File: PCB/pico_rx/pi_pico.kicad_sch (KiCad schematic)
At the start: 18 parts, among them J3 Battery, J3 Speaker, J4 Headphone, J4 I2C Display, SW1 RotaryEncoder_Switch, SW1 SW_Push, SW2 SW_Push, SW4 SW_SPDT, U5 Pico

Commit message: Get CW working
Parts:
- added R3 (x2): 1k, Resistor_SMD:R_0805_2012Metric, symbol Device:R
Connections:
- net RX_I: now also R3.2; no longer U5.32 (GPIO27_ADC1)
- net RX_Q: now also R3.2; no longer U5.31 (GPIO26_ADC0)
- net PUSH: now reaches U5.7 (GPIO5)
- net PUSH: now also SW1.S1
- net EEPROM_SCL: no longer names the net of U5.20 (GPIO15)
- net EEPROM_SDA: no longer names the net of U5.19 (GPIO14)
- new net: R3.1, U5.31 (GPIO26_ADC0)
- new net: R3.1, U5.32 (GPIO27_ADC1)
- no-connect marks 0 -> 21
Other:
- note added: "Note: D1 must be removed from PI Pico"
- note added: "R9, C34 determine LPF cutoff 1/(2 * pi * 100 * 100e-9) ~= 16kHz"
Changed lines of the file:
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@@
   (junction (at 217.17 96.52) (diameter 0) (color 0 0 0 0)
   )
+  (no_connect (at 52.07 66.04))
+  (no_connect (at 142.24 106.68))
+  (no_connect (at 160.02 53.34))
+  (no_connect (at 160.02 68.58))
+  (no_connect (at 160.02 60.96))
+  (no_connect (at 160.02 78.74))
+  (no_connect (at 124.46 81.28))
+  (no_connect (at 124.46 99.06))
+  (no_connect (at 124.46 88.9))
+  (no_connect (at 124.46 93.98))
+  (no_connect (at 124.46 78.74))
+  (no_connect (at 88.9 166.37))
+  (no_connect (at 124.46 91.44))
+  (no_connect (at 139.7 106.68))
+  (no_connect (at 124.46 101.6))
+  (no_connect (at 160.02 71.12))
+  (no_connect (at 144.78 106.68))
+  (no_connect (at 124.46 73.66))
+  (no_connect (at 124.46 86.36))
+  (no_connect (at 124.46 76.2))
+  (no_connect (at 160.02 66.04))
   (wire (pts (xy 176.53 55.88) (xy 171.45 55.88))
     (stroke (width 0) (type default))
@@
     (stroke (width 0) (type default))
   )
-  (wire (pts (xy 107.95 101.6) (xy 124.46 101.6))
-    (stroke (width 0) (type default))
-  )
   (wire (pts (xy 160.02 58.42) (xy 165.1 58.42))
     (stroke (width 0) (type default))
@@
     (stroke (width 0) (type default))
   )
+  (wire (pts (xy 234.95 86.36) (xy 238.76 86.36))
+    (stroke (width 0) (type default))
+  )
   (wire (pts (xy 36.83 66.04) (xy 40.64 66.04))
     (stroke (width 0) (type default))
@@
     (stroke (width 0) (type default))
   )
+  (wire (pts (xy 179.07 76.2) (xy 182.88 76.2))
+    (stroke (width 0) (type default))
+  )
   (wire (pts (xy 238.76 96.52) (xy 217.17 96.52))
     (stroke (width 0) (type default))
@@
     (stroke (width 0) (type default))
   )
-  (wire (pts (xy 189.23 91.44) (xy 189.23 88.9))
-    (stroke (width 0) (type default))
-  )
   (wire (pts (xy 81.28 179.07) (xy 82.55 179.07))
     (stroke (width 0) (type default))
@@
     (stroke (width 0) (type default))
   )
+  (wire (pts (xy 179.07 73.66) (xy 182.88 73.66))
+    (stroke (width 0) (type default))
+  )
   (wire (pts (xy 105.41 63.5) (xy 124.46 63.5))
     (stroke (width 0) (type default))
@@
     (stroke (width 0) (type default))
   )
+  (wire (pts (xy 95.25 68.58) (xy 124.46 68.58))
+    (stroke (width 0) (type default))
+  )
   (wire (pts (xy 165.1 83.82) (xy 165.1 96.52))
     (stroke (width 0) (type default))
@@
   )
   (wire (pts (xy 217.17 140.97) (xy 223.52 140.97))
-    (stroke (width 0) (type default))
-  )
-  (wire (pts (xy 107.95 99.06) (xy 124.46 99.06))
     (stroke (width 0) (type default))
   )
@@
     (effects (font (size 1.27 1.27)) (justify right bottom))
   )
+  (text "Note: D1 must be removed from PI Pico" (at 121.92 43.18 0)
+    (effects (font (size 1.27 1.27)) (justify left bottom))
+  )
   (text "User Interface" (at 198.12 40.64 0)
     (effects (font (size 1.27 1.27)) (justify left bottom))
   )
-  (label "EEPROM_SCL" (at 107.95 101.6 180) (fields_autoplaced)
-    (effects (font (size 1.27 1.27)) (justify right bottom))
+  (text "R9, C34  determine LPF cutoff\n1/(2 * pi * 100 * 100e-9) ~= 16kHz"
+    (at 21.59 148.59 0)
+    (effects (font (size 2.5 2.5)) (justify left bottom))
+  )
+  (label "PUSH" (at 238.76 86.36 0) (fields_autoplaced)
+    (effects (font (size 1.27 1.27)) (justify left bottom))
   )
   (label "BUTTON_BACK" (at 172.72 99.06 0) (fields_autoplaced)
@@
     (effects (font (size 1.27 1.27)) (justify right bottom))
   )
-  (label "EEPROM_SDA" (at 107.95 99.06 180) (fields_autoplaced)
-    (effects (font (size 1.27 1.27)) (justify right bottom))
-  )
   (label "SCL" (at 172.72 91.44 0) (fields_autoplaced)
     (effects (font (size 1.27 1.27)) (justify left bottom))
   )
+  (label "PUSH" (at 95.25 68.58 180) (fields_autoplaced)
+    (effects (font (size 1.27 1.27)) (justify right bottom))
+  )
   (label "BUTTON_FWD" (at 172.72 81.28 0) (fields_autoplaced)
     (effects (font (size 1.27 1.27)) (justify left bottom))
@@
     (effects (font (size 1.27 1.27)) (justify right bottom))
   )
-  (global_label "RX_I" (shape input) (at 171.45 73.66 0) (fields_autoplaced)
+  (global_label "RX_I" (shape input) (at 182.88 73.66 0) (fields_autoplaced)
     (effects (font (size 1.27 1.27)) (justify left))
-    (property "Intersheetrefs" "${INTERSHEET_REFS}" (at 178.4871 73.66 0)
+    (property "Intersheetrefs" "${INTERSHEET_REFS}" (at 189.9171 73.66 0)
       (effects (font (size 1.27 1.27)) (justify left) hide)
     )
@@
     )
   )
-  (global_label "RX_Q" (shape input) (at 171.45 76.2 0) (fields_autoplaced)
+  (global_label "RX_Q" (shape input) (at 182.88 76.2 0) (fields_autoplaced)
     (effects (font (size 1.27 1.27)) (justify left))
-    (property "Intersheetrefs" "${INTERSHEET_REFS}" (at 179.2128 76.2 0)
+    (property "Intersheetrefs" "${INTERSHEET_REFS}" (at 190.6428 76.2 0)
       (effects (font (size 1.27 1.27)) (justify left) hide)
     )
@@
     )
   )
-  (symbol (lib_id "Device:R") (at 48.26 168.91 90) (unit 1)
-    (in_bom yes) (on_board yes) (dnp no)
-    (property "Reference" "R3" (at 48.26 163.6776 90)
-      (effects (font (size 1.27 1.27)))
-    )
-    (property "Value" "100" (at 48.26 165.989 90)
-      (effects (font (size 1.27 1.27)))
-    )
-    (property "Footprint" "Resistor_SMD:R_0805_2012Metric" (at 48.26 170.688 90)
-      (effects (font (size 1.27 1.27)) hide)
-    )
-    (property "Datasheet" "~" (at 48.26 168.91 0)
+  (symbol (lib_id "Device:R") (at 175.26 76.2 90) (unit 1)
+    (in_bom yes) (on_board yes) (dnp no)
+    (property "Reference" "R3" (at 167.64 80.01 90)
+      (effects (font (size 1.27 1.27)))
+    )
+    (property "Value" "1k" (at 167.64 77.47 90)
+      (effects (font (size 1.27 1.27)))
+    )
+    (property "Footprint" "Resistor_SMD:R_0805_2012Metric" (at 175.26 77.978 90)
+      (effects (font (size 1.27 1.27)) hide)
+    )
+    (property "Datasheet" "~" (at 175.26 76.2 0)
       (effects (font (size 1.27 1.27)) hide)
     )
@@
       (project "pico_rx"
         (path "/b6f73a49-ac1f-4895-a0f9-8f6954ee587f/ef5e145d-7cd2-41fd-85f8-55f3445b8dc3"
+          (reference "R14") (unit 1)
+        )
+      )
+    )
+  )
+  (symbol (lib_id "Device:R") (at 48.26 168.91 90) (unit 1)
+    (in_bom yes) (on_board yes) (dnp no)
+    (property "Reference" "R3" (at 48.26 163.6776 90)
+      (effects (font (size 1.27 1.27)))
+    )
+    (property "Value" "100" (at 48.26 165.989 90)
+      (effects (font (size 1.27 1.27)))
+    )
+    (property "Footprint" "Resistor_SMD:R_0805_2012Metric" (at 48.26 170.688 90)
+      (effects (font (size 1.27 1.27)) hide)
+    )
+    (property "Datasheet" "~" (at 48.26 168.91 0)
+      (effects (font (size 1.27 1.27)) hide)
+    )
+    (pin "1")
+    (pin "2")
+    (instances
+      (project "RADIO"
+        (path "/852d5a42-8663-46cd-bbc7-538bfe8c017d/00000000-0000-0000-0000-00005e371e22"
+          (reference "R3") (unit 1)
+        )
+      )
+      (project "pico_rx"
+        (path "/b6f73a49-ac1f-4895-a0f9-8f6954ee587f/ef5e145d-7cd2-41fd-85f8-55f3445b8dc3"
           (reference "R9") (unit 1)
         )
@@
         )
       )
+    )
+  )
+  (symbol (lib_id "Device:R") (at 175.26 73.66 90) (unit 1)
+    (in_bom yes) (on_board yes) (dnp no)
+    (property "Reference" "R3" (at 167.64 72.39 90)
+      (effects (font (size 1.27 1.27)))
+    )
+    (property "Value" "1k" (at 167.64 69.85 90)
+      (effects (font (size 1.27 1.27)))
+    )
+    (property "Footprint" "Resistor_SMD:R_0805_2012Metric" (at 175.26 75.438 90)
+      (effects (font (size 1.27 1.27)) hide)
+    )
+    (property "Datasheet" "~" (at 175.26 73.66 0)
+      (effects (font (size 1.27 1.27)) hide)
+    )
+    (pin "1")
+    (pin "2")
+    (instances
+      (project "RADIO"
+        (path "/852d5a42-8663-46cd-bbc7-538bfe8c017d/00000000-0000-0000-0000-00005e371e22"
+          (reference "R3") (unit 1)
+        )
+      )
+      (project "pico_rx"
+        (path "/b6f73a49-ac1f-4895-a0f9-8f6954ee587f/ef5e145d-7cd2-41fd-85f8-55f3445b8dc3"
+          (reference "R13") (unit 1)
+        )
+      )

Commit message: Prepare PCB for manufacture
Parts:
- added R3 (x2): 1k, Resistor_SMD:R_0805_2012Metric, symbol Device:R
- C53: footprint Capacitor_Tantalum_SMD:CP_EIA-7343-31_Kemet-D -> Capacitor_Tantalum_SMD:CP_EIA-3528-21_Kemet-B
- R3: value 1k -> 470
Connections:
- net GND: now also R3.1, R3.1
- net at R3.1, U5.31 (GPIO26_ADC0): now also R3.2
- net at R3.1, U5.32 (GPIO27_ADC1): now also R3.2
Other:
- moved on the sheet: J4, R3, SW1, SW2

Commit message: Update power calculation
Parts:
- C9: value 100n -> 470n
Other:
- note added: "R9, C34 determine LPF cutoff 1/(2 * pi * 100 * 470e-9) ~= 3kHz"
- note removed: "R9, C34 determine LPF cutoff 1/(2 * pi * 100 * 100e-9) ~= 16kHz"
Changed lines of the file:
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@@
     (effects (font (size 1.27 1.27)) (justify left bottom))
   )
-  (text "R9, C34  determine LPF cutoff\n1/(2 * pi * 100 * 100e-9) ~= 16kHz"
+  (text "R9, C34  determine LPF cutoff\n1/(2 * pi * 100 * 470e-9) ~= 3kHz"
     (at 21.59 148.59 0)
     (effects (font (size 2.5 2.5)) (justify left bottom))
@@
       (effects (font (size 1.27 1.27)) (justify left))
     )
-    (property "Value" "100n" (at 62.611 176.403 0)
+    (property "Value" "470n" (at 62.611 176.403 0)
       (effects (font (size 1.27 1.27)) (justify left))
     )

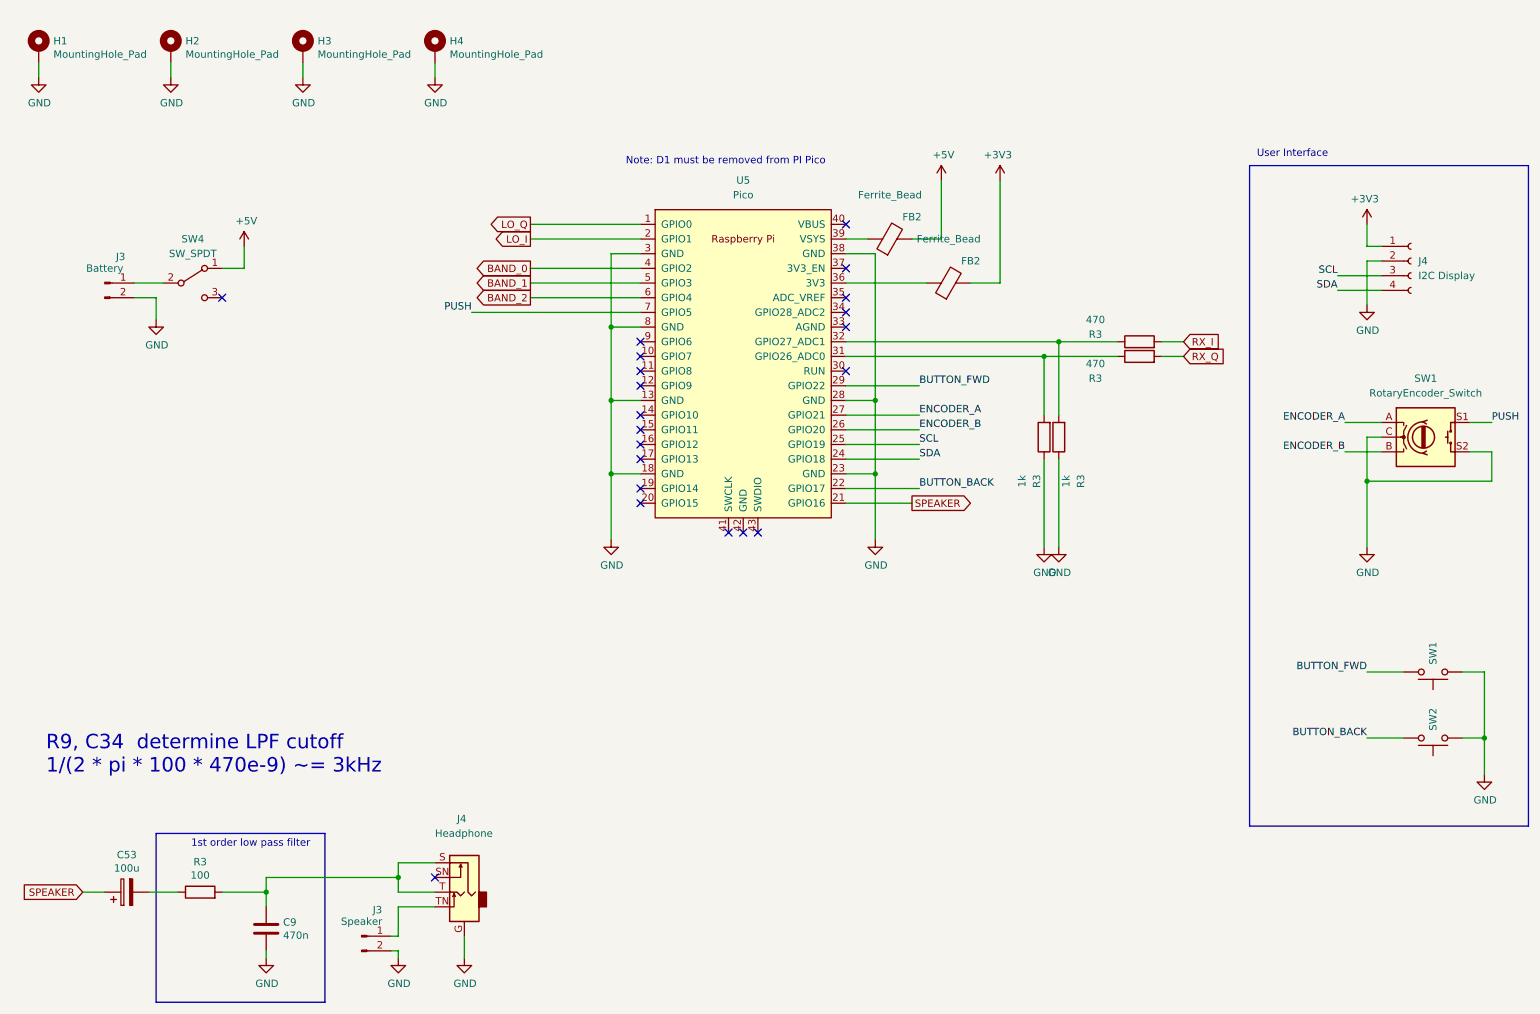
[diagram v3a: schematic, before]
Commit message: Improve frequency resolution by making small adjustments to system clock. Add utility to upload memory contents over USB
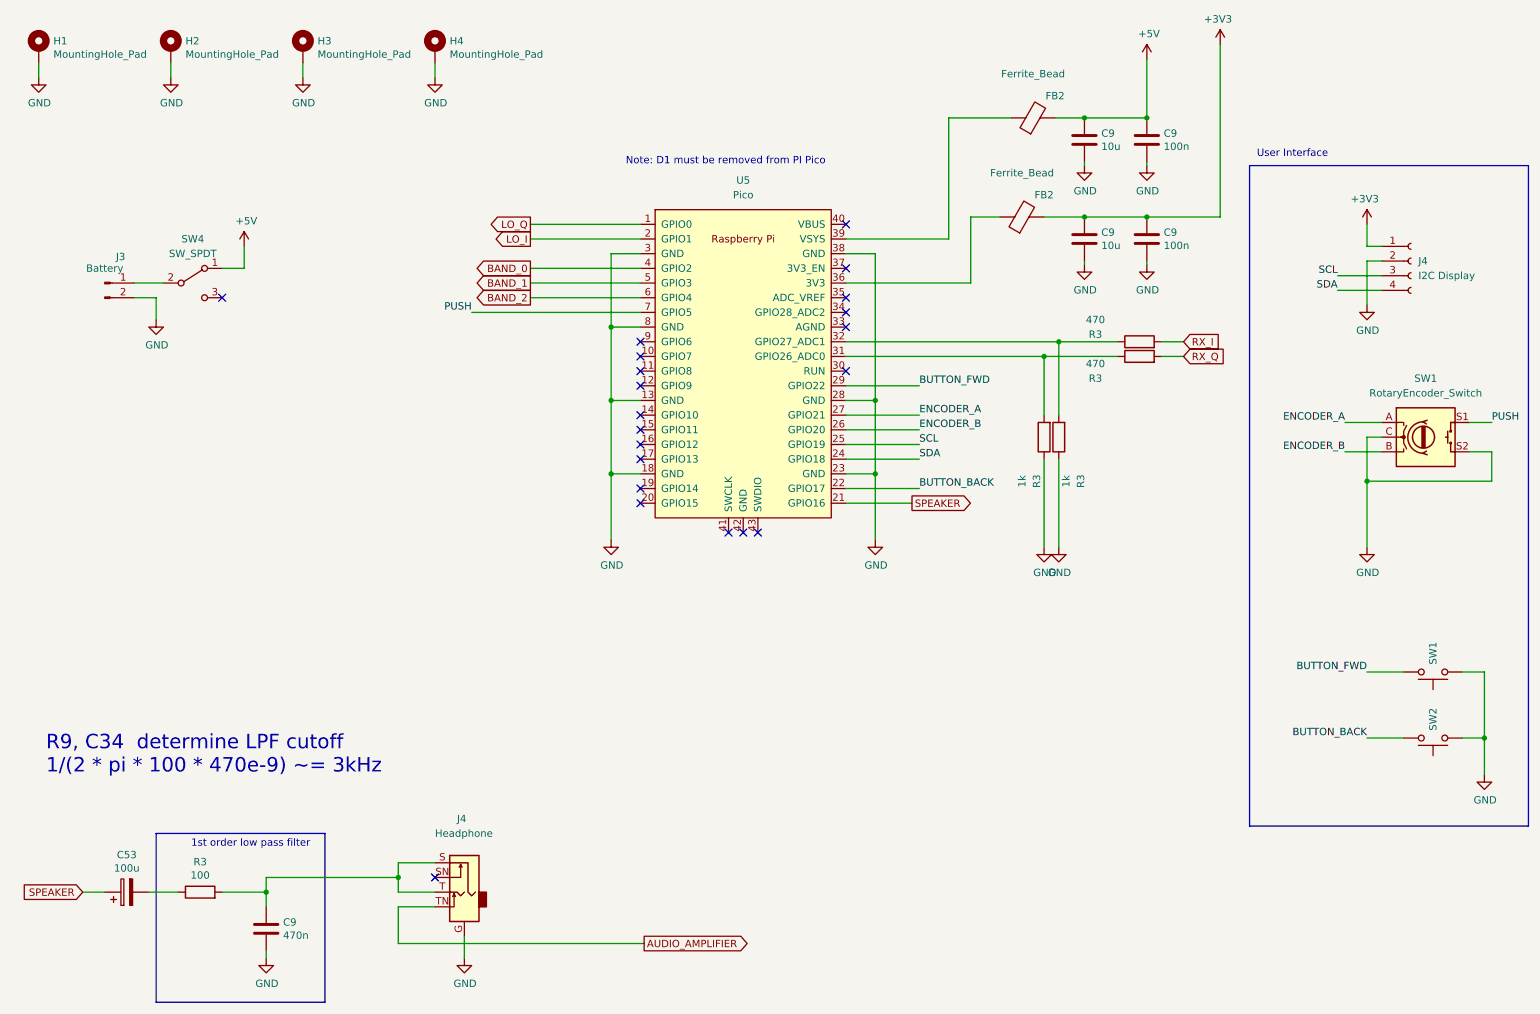
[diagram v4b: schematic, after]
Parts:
- removed J3: Speaker, Connector_PinHeader_2.54mm:PinHeader_1x02_P2.54mm_Vertical, symbol RADIO-rescue:Conn_01x02_Male-Connector
- added C9 (x2): 10u, Capacitor_SMD:C_0805_2012Metric, symbol Device:C
- added C9 (x2): 100n, Capacitor_SMD:C_0805_2012Metric, symbol Device:C
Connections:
- net +3V3: now also C9.1, C9.1
- net +5V: now also C9.1, C9.1
- net GND: now also C9.2, C9.2, C9.2, C9.2
- net AUDIO_AMPLIFIER: now reaches J4.TN
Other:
- moved on the sheet: FB2

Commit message: Update PCB design to fix issues found
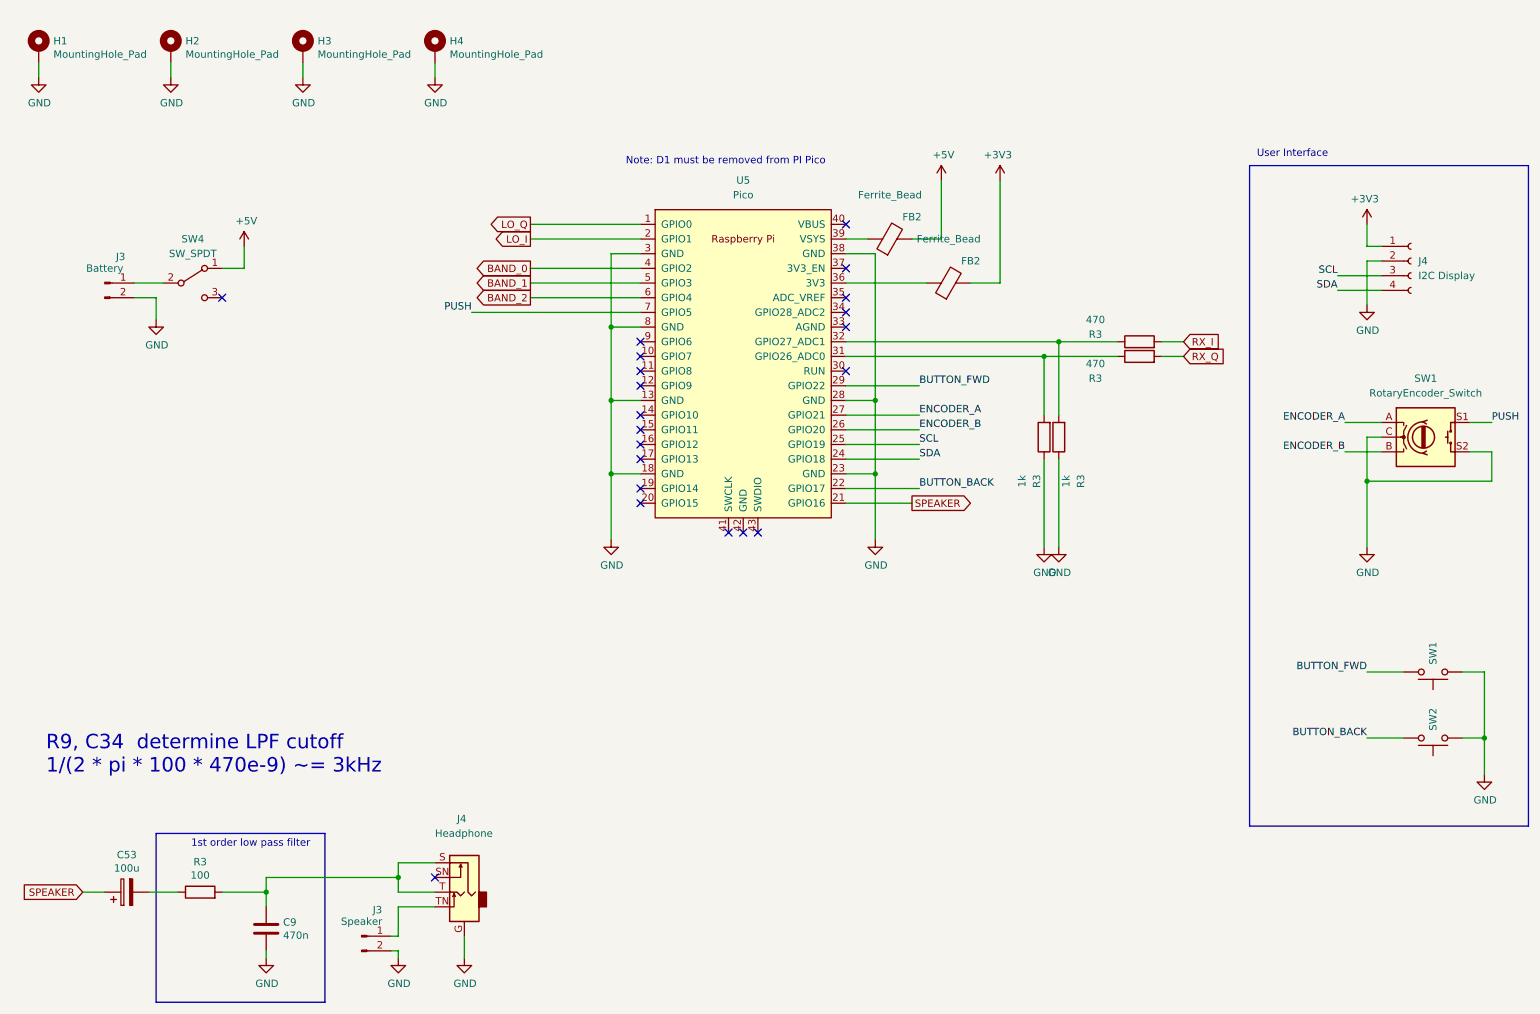
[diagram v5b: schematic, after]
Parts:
- removed C9 (x2): 10u, Capacitor_SMD:C_0805_2012Metric, symbol Device:C
- removed C9 (x2): 100n, Capacitor_SMD:C_0805_2012Metric, symbol Device:C
- added J3: Speaker, Connector_PinHeader_2.54mm:PinHeader_1x02_P2.54mm_Vertical, symbol RADIO-rescue:Conn_01x02_Male-Connector
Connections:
- net GND: now also J3.2 (Pin_2)
- net AUDIO_AMPLIFIER: no longer names the net of J4.TN
- net AUDIO_AMPLIFIER: now also J3.1 (Pin_1)
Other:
- moved on the sheet: FB2
